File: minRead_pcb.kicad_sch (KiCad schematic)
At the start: 136 parts, among them J1 USB_C_Receptacle, J2 FH34SRJ-24S-0.5SH_50_, J3 FH34SRJ-6S-0.5SH_50_, J5 Conn_01x02, J6 PPPC062LJBN-RC, J7 Micro_SD_Card, Q1 FS8205A, Q10 BSS138, Q11 BSS138, Q16 MMBT3906, Q17 MMBT3904, Q18 AO3419, Q3 AO3419, Q4 [BSS138] AO3400A, Q8 AO3419, SW1 SW_Push, SW10 SW_Push, SW11 SW_Push, SW2 SW_Push, SW3 SW_Push, SW4 SW_Push, SW5 SW_Push, SW6 SW_Push, SW7 SW_Push, SW8 SW_Push, SW9 SW_Push, U1 TPD4E1U06DBVR, U11 AP3031KTR, U2 TPS2116DRL, U3 AP2112K-3.3, U4 ESP32-S3-WROOM-1, U5 DW01A, U6 TPD4E1U06DBVR, U7 MCP73832-2-OT, U8 TPD4E1U06DBVR, U9 TPD4E1U06DBVR

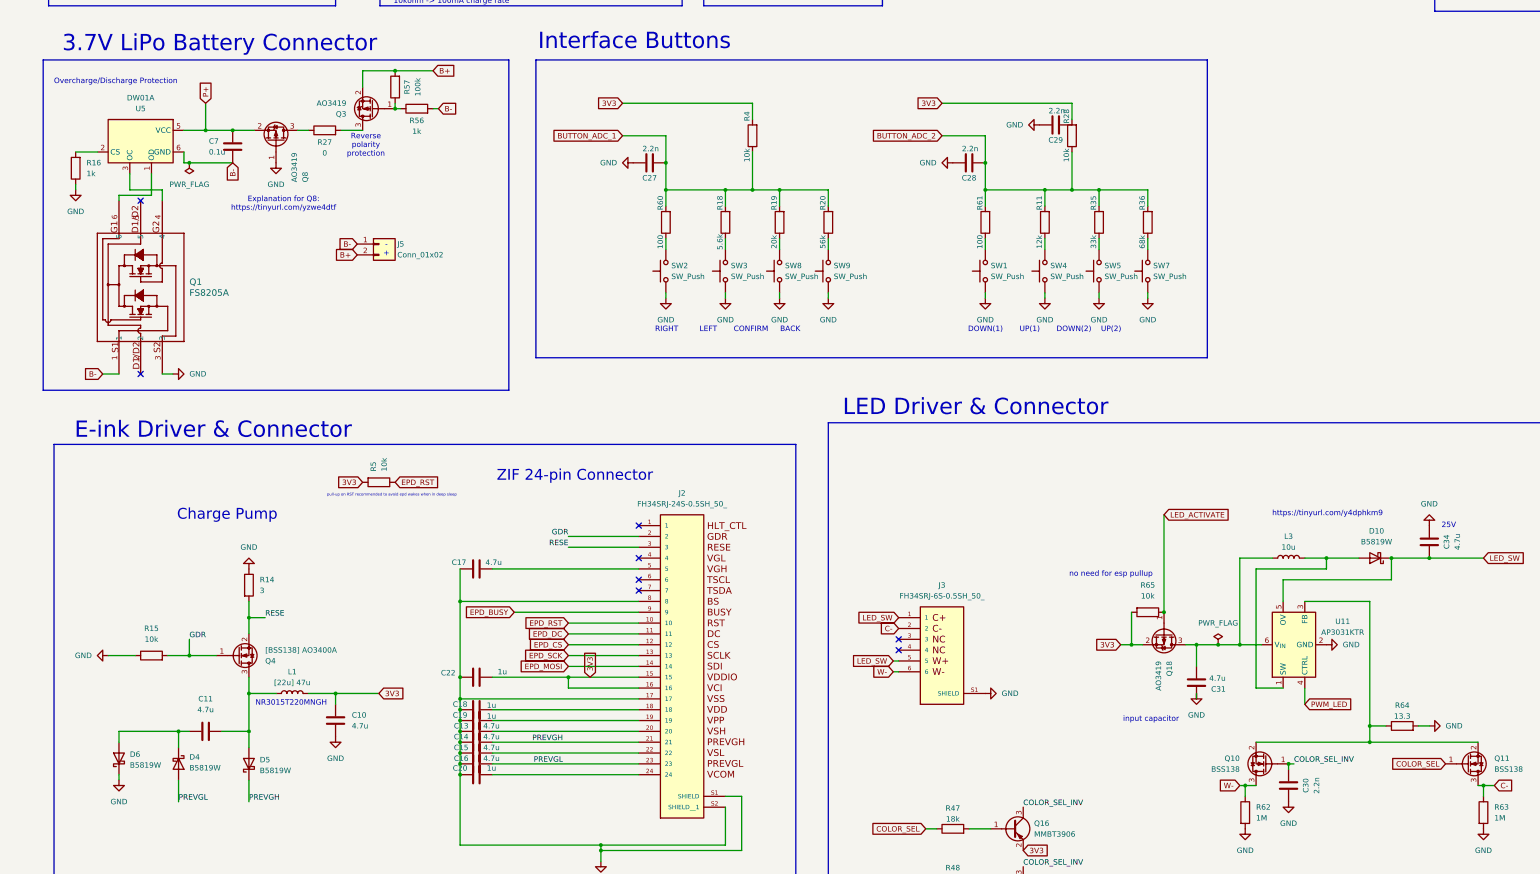
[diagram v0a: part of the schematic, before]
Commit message: remove left buttons, begin simplifying charge circuit
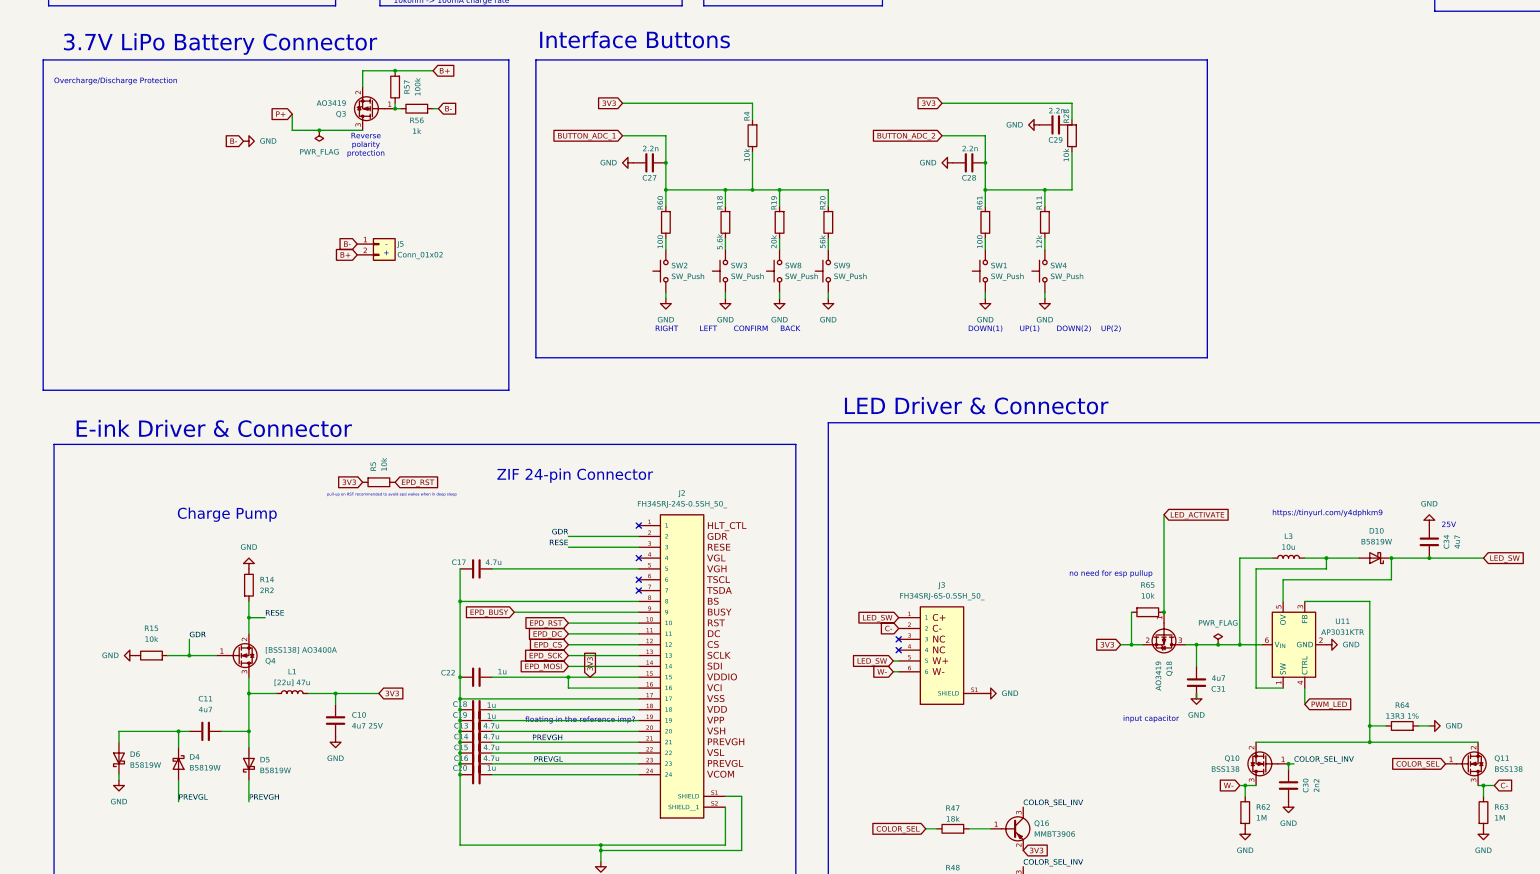
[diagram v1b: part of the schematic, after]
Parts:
- removed C7: 0.1u, Capacitor_SMD:C_0805_2012Metric_Pad1.18x1.45mm_HandSolder, symbol Device:C
- removed Q1: FS8205A, Package_TO_SOT_SMD:SOT-23-6_Handsoldering, symbol FS8205A:FS8205A
- removed Q8: AO3419, Package_TO_SOT_SMD:SOT-23_Handsoldering, symbol Transistor_FET:IRLML6402
- removed R16: 1k, Resistor_SMD:R_0805_2012Metric_Pad1.20x1.40mm_HandSolder, symbol Device:R
- removed R27: 0, Resistor_SMD:R_0805_2012Metric_Pad1.20x1.40mm_HandSolder, symbol Device:R
- removed R35: 33k, Resistor_SMD:R_0805_2012Metric_Pad1.20x1.40mm_HandSolder, symbol Device:R
- removed R36: 68k, Resistor_SMD:R_0805_2012Metric_Pad1.20x1.40mm_HandSolder, symbol Device:R
- removed SW5, SW7: SW_Push, mjtp1117:MJTP1117, symbol Switch:SW_Push
- removed U5: DW01A, Package_TO_SOT_SMD:SOT-23-6_Handsoldering, symbol Battery_Management:DW01A
- C10: value 4.7u -> 4u7 25V
- C11, C31, C34: value 4.7u -> 4u7
- C30: value 2.2n -> 2n2
- R14: value 3 -> 2R2
- R64: value 13.3 -> 13R3 1%
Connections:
- net B- is gone; now on net GND: J5.1 (Pin_1), R56.2
- net P+: now also Q3.3 (D)
- no-connect marks 13 -> 11
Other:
- note added: "floating in the reference imp?"
- note removed: "Explanation for Q8:"
- note removed: "NR3015T220MNGH"
- note removed: "https://tinyurl.com/yzwe4dtf"

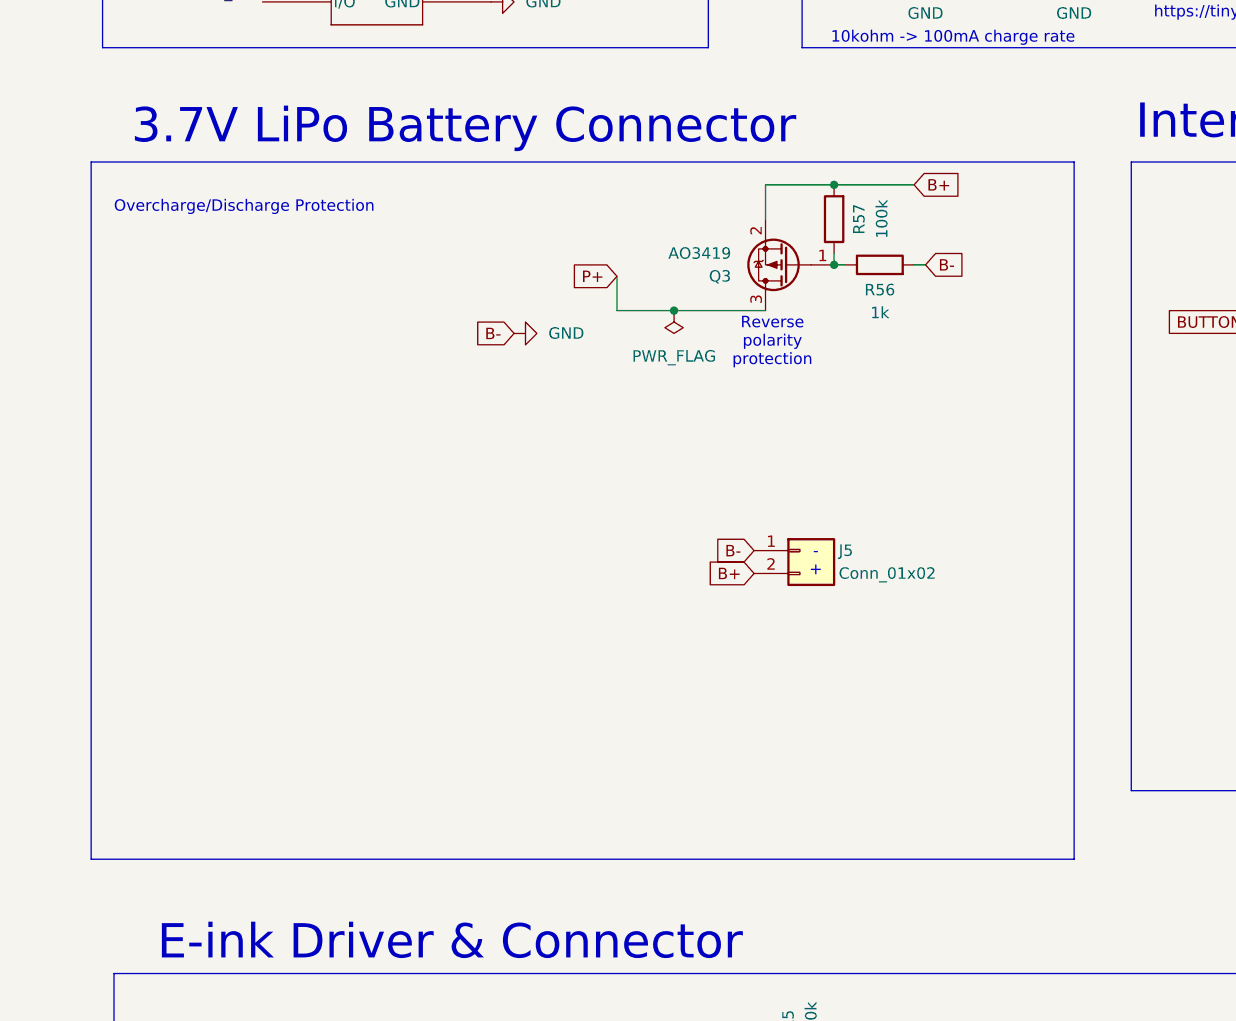
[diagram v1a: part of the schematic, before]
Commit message: charge circuit removed overcharge protection
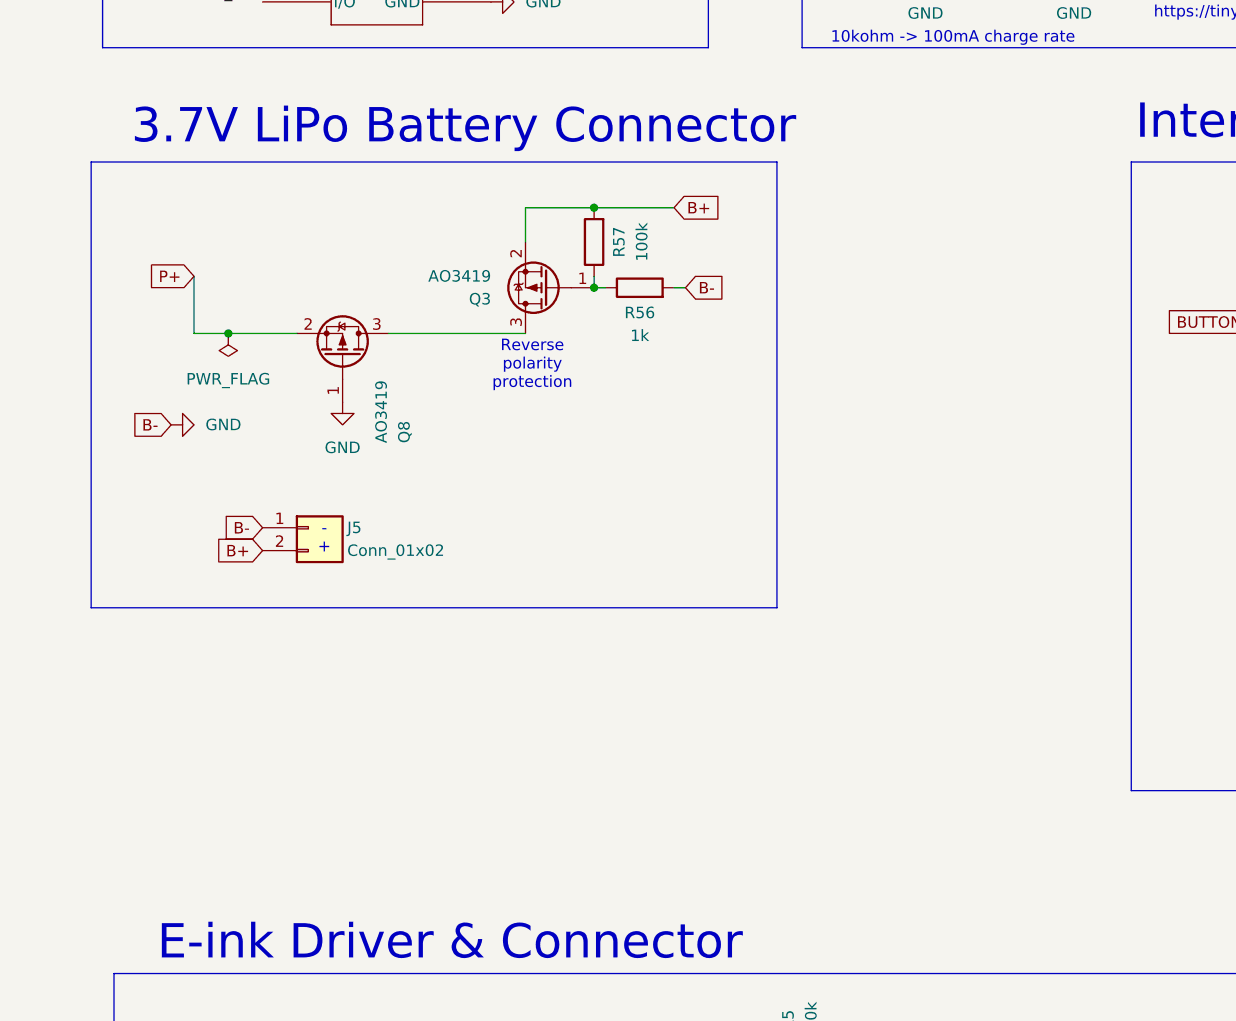
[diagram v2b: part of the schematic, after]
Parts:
- added Q8: AO3419, Package_TO_SOT_SMD:SOT-23_Handsoldering, symbol Transistor_FET:IRLML6402
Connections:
- net GND: now also Q8.1 (G)
- net P+: now also Q8.2 (S); no longer Q3.3 (D)
- new net: Q3.3 (D), Q8.3 (D)
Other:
- note removed: "Overcharge/Discharge Protection"
- moved on the sheet: J5, Q3, R56, R57

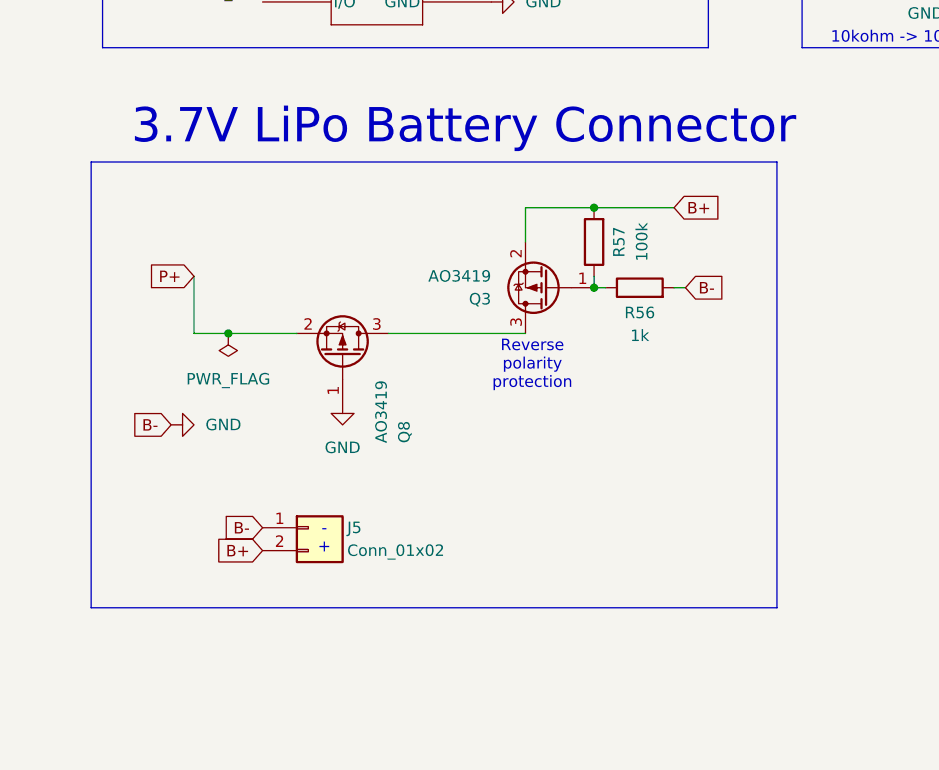
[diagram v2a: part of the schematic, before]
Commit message: simplify reverse polarity circuit
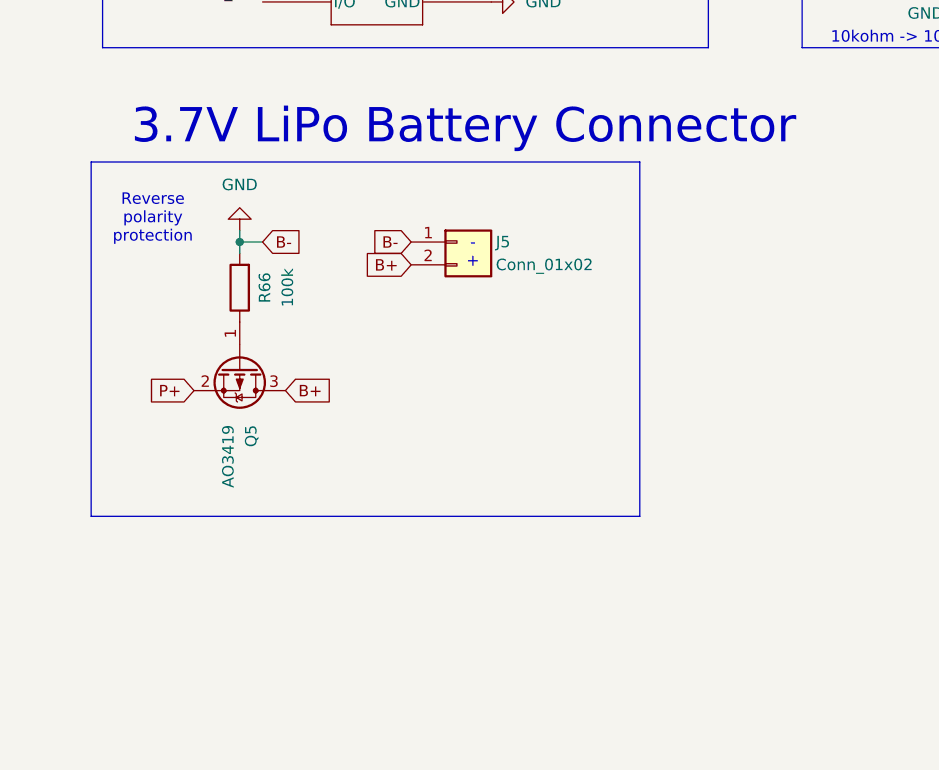
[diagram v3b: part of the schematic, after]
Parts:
- removed Q3, Q8: AO3419, Package_TO_SOT_SMD:SOT-23_Handsoldering, symbol Transistor_FET:IRLML6402
- removed R56: 1k, Resistor_SMD:R_0805_2012Metric_Pad1.20x1.40mm_HandSolder, symbol Device:R
- removed R57: 100k, Resistor_SMD:R_0805_2012Metric_Pad1.20x1.40mm_HandSolder, symbol Device:R
- added Q5: AO3419, Package_TO_SOT_SMD:SOT-23_Handsoldering, symbol Transistor_FET:IRLML6402
- added R66: 100k, Resistor_SMD:R_0805_2012Metric_Pad1.20x1.40mm_HandSolder, symbol Device:R
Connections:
- net B+: now also Q5.3 (D)
- net GND: now also R66.2
- net P+: now also Q5.2 (S)
- new net: Q5.1 (G), R66.1
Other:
- moved on the sheet: J5

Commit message: remove external peripheral port
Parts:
- removed CR2: TSD05CDYFR, Diode_SMD:D_SOD-323_HandSoldering, symbol TSD05CDYFR:TSD05CDYFR
- removed D3: SMAJ30A, Diode_SMD:D_SMA, symbol Diode:SMAJ30A
- removed D8: PESD2IVN-UX, Package_TO_SOT_SMD:SOT-323_SC-70_Handsoldering, symbol Device:D_TVS_Dual_ACA
- removed J6: PPPC062LJBN-RC, PPPC_12:CONN_PPPC062LJBN-RC_SUL, symbol PPPC_12:PPPC062LJBN-RC
- removed U8, U9: TPD4E1U06DBVR, Package_TO_SOT_SMD:SOT-23-6_Handsoldering, symbol TPD4E1U06DBVR:TPD4E1U06DBVR
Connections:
- net RX: no longer names the net of U4.36 (RXD0)
- net TX: no longer names the net of U4.37 (TXD0)
- no-connect marks 11 -> 10
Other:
- note added: "consider longer sampling time to compensate for high resistance"
- note removed: "External Peripheral Connector"
- note removed: "External Peripheral ESD Protection"
- moved on the sheet: C30, C31, C32, C33, C34, C5, D10, L3, Q10, Q11, Q18, R13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

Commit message: general cleanup and notation
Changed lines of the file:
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@@
 	(wire
 		(pts
-			(xy 144.78 41.91) (xy 144.78 44.45)
-		)
-		(stroke
-			(width 0)
-			(type default)
-		)
-	)
-	(wire
-		(pts
 			(xy 142.24 85.09) (xy 142.24 83.82)
 		)
@@
 					(unit 1)
 				)
-			)
-		)
-	)
-	(symbol
-		(lib_id "power:PWR_FLAG")
-		(at 144.78 41.91 0)
-		(unit 1)
-		(body_style 1)
-		(exclude_from_sim no)
-		(in_bom yes)
-		(on_board yes)
-		(in_pos_files yes)
-		(dnp no)
-		(fields_autoplaced yes)
-		(property "Reference" "#FLG02"
-			(at 144.78 40.005 0)
-			(hide yes)
-			(show_name no)
-			(do_not_autoplace no)
-			(effects
-				(font
-					(size 1.27 1.27)
-				)
-			)
-		)
-		(property "Value" "PWR_FLAG"
-			(at 147.32 40.6399 0)
-			(show_name no)
-			(do_not_autoplace no)
-			(effects
-				(font
-					(size 1.27 1.27)
-				)
-				(justify left)
-			)
-		)
-		(property "Footprint" ""
-			(at 144.78 41.91 0)
-			(hide yes)
-			(show_name no)
-			(do_not_autoplace no)
-			(effects
-				(font
-					(size 1.27 1.27)
-				)
-			)
-		)
-		(property "Datasheet" ""
-			(at 144.78 41.91 0)
-			(hide yes)
-			(show_name no)
-			(do_not_autoplace no)
-			(effects
-				(font
-					(size 1.27 1.27)
-				)
-			)
-		)
-		(property "Description" "Special symbol for telling ERC where power comes from"
-			(at 144.78 41.91 0)
-			(hide yes)
-			(show_name no)
-			(do_not_autoplace no)
-			(effects
-				(font
-					(size 1.27 1.27)
-				)
-			)
-		)
-		(pin "1"
-		)
-		(instances
-			(project "minRead_pcb"
-				(path "/2fbd4c8f-b784-4d80-b374-4947df99a9bf"
-					(reference "#FLG02")
-					(unit 1)
-				)

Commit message: pre-simplify
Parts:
- J5: footprint Connector_JST:JST_PH_S2B-PH-K_1x02_P2.00mm_Horizontal -> DEAN:Battery pads
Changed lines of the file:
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@@
+		(length 2.54)
+		(shape round)
+		(at 48.26 30.48 180)
+		(fields_autoplaced yes)
+		(effects
+			(font
+				(size 1.27 1.27)
+			)
+			(justify right bottom)
+		)
+		(property "Netclass" "3V3"
+			(at 48.9585 33.02 0)
+			(show_name no)
+			(do_not_autoplace no)
+			(effects
+				(font
+					(size 1.27 1.27)
+				)
+				(justify left)
+			)
+		)
+		(property "Component Class" ""
+			(at -171.45 -219.71 0)
+			(show_name no)
+			(do_not_autoplace no)
+			(effects
+				(font
+					(size 1.27 1.27)
+					(italic yes)
+				)
+			)
+		)
+	)
+	(netclass_flag ""
 		(length 2.54)
 		(shape round)
@@
 			(justify right bottom)
 		)
-		(property "Netclass" "15V"
+		(property "Netclass" "3V3"
 			(at 294.0685 302.26 0)
 			(show_name no)
@@
 		(length 2.54)
 		(shape round)
-		(at 304.8 289.56 0)
+		(at 58.42 30.48 180)
 		(fields_autoplaced yes)
 		(effects
@@
 				(size 1.27 1.27)
 			)
+			(justify right bottom)
+		)
+		(property "Netclass" "3V3"
+			(at 59.1185 33.02 0)
+			(show_name no)
+			(do_not_autoplace no)
+			(effects
+				(font
+					(size 1.27 1.27)
+				)
+				(justify left)
+			)
+		)
+		(property "Component Class" ""
+			(at -161.29 -219.71 0)
+			(show_name no)
+			(do_not_autoplace no)
+			(effects
+				(font
+					(size 1.27 1.27)
+					(italic yes)
+				)
+			)
+		)
+	)
+	(netclass_flag ""
+		(length 2.54)
+		(shape round)
+		(at 304.8 289.56 0)
+		(fields_autoplaced yes)
+		(effects
+			(font
+				(size 1.27 1.27)
+			)
 			(justify left bottom)
 		)
-		(property "Netclass" "15V"
+		(property "Netclass" "3V3"
 			(at 305.4985 287.02 0)
 			(show_name no)
@@
 			(justify left bottom)
 		)
-		(property "Netclass" "15V"
+		(property "Netclass" "3V3"
 			(at 347.4085 297.18 0)
 			(show_name no)
@@
 			)
 		)
-		(property "Footprint" "Connector_JST:JST_PH_S2B-PH-K_1x02_P2.00mm_Horizontal"
+		(property "Footprint" "DEAN:Battery pads"
 			(at 58.42 148.59 0)
 			(hide yes)
